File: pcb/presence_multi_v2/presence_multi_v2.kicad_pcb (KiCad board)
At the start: 2 copper layers, 27 parts, among them J1 USB_C_Receptacle_USB2.0_16P, J2 TC2050, J3 Conn_01x06_Socket, U2 AMS1117-3.3, U3 CH340E, Y1 Wurth 830050789

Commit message: replaced ASM1117 with LDL1117, removed 8 pin socket, added 3 4-pin JST-PH connectors
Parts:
- removed ES1: ENS160+AHT21, Connector_PinSocket_2.54mm:PinSocket_1x08_P2.54mm_Vertical
- removed U2: AMS1117-3.3, Package_TO_SOT_SMD:SOT-223-3_TabPin2
- added I2C_Ext1: JST-PH 1x4 2.0, Connector_JST:JST_PH_B4B-PH-K_1x04_P2.00mm_Vertical, F.Cu at (126.5, 125.0)
- added I2C_Ext2: JST-PH 1x4 2.0, Connector_JST:JST_PH_B4B-PH-K_1x04_P2.00mm_Vertical, F.Cu at (136.3, 125.0)
- added I2C_Ext3: JST-PH 1x4 2.0, Connector_JST:JST_PH_B4B-PH-K_1x04_P2.00mm_Vertical, F.Cu at (146.3, 125.0)
- added IC1: LDL1117S33R, theorlangur:LDL1117S33R, F.Cu at (138.0, 100.0)
- C5: value 22u -> 10u
- moved C5 12.0 mm to (132.7, 101.2)
- moved C4 1.25 mm to (143.7, 98.4)
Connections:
- C4 pad 1: /LDO_IN -> GND
- C4 pad 2: GND -> /LDO_IN
- MCU1 pad 20: /I_AIR1 -> unconnected-(MCU1-P1.07/AIN3-Pad20)

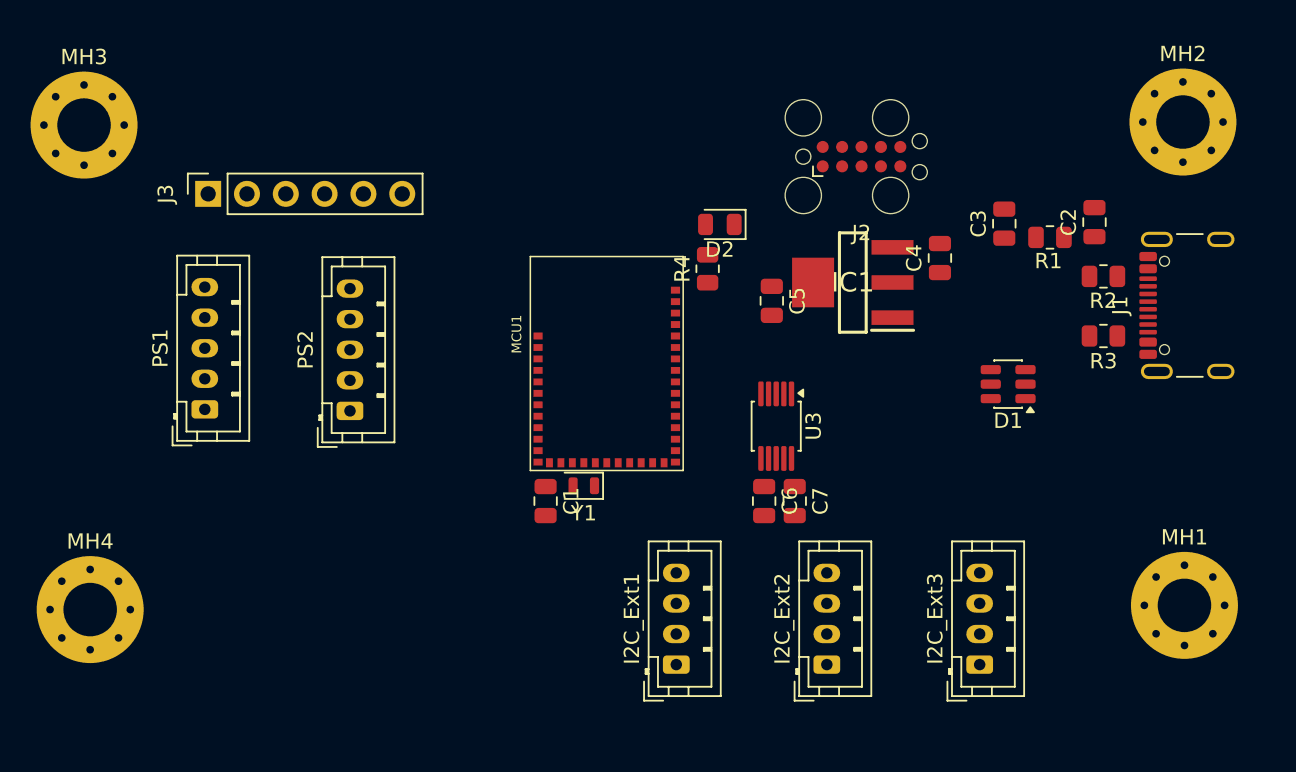
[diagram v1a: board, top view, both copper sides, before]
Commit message: added buttons, configured PCB settings
removed layers
configured pre-defined ruls (constraints)
added default sizes
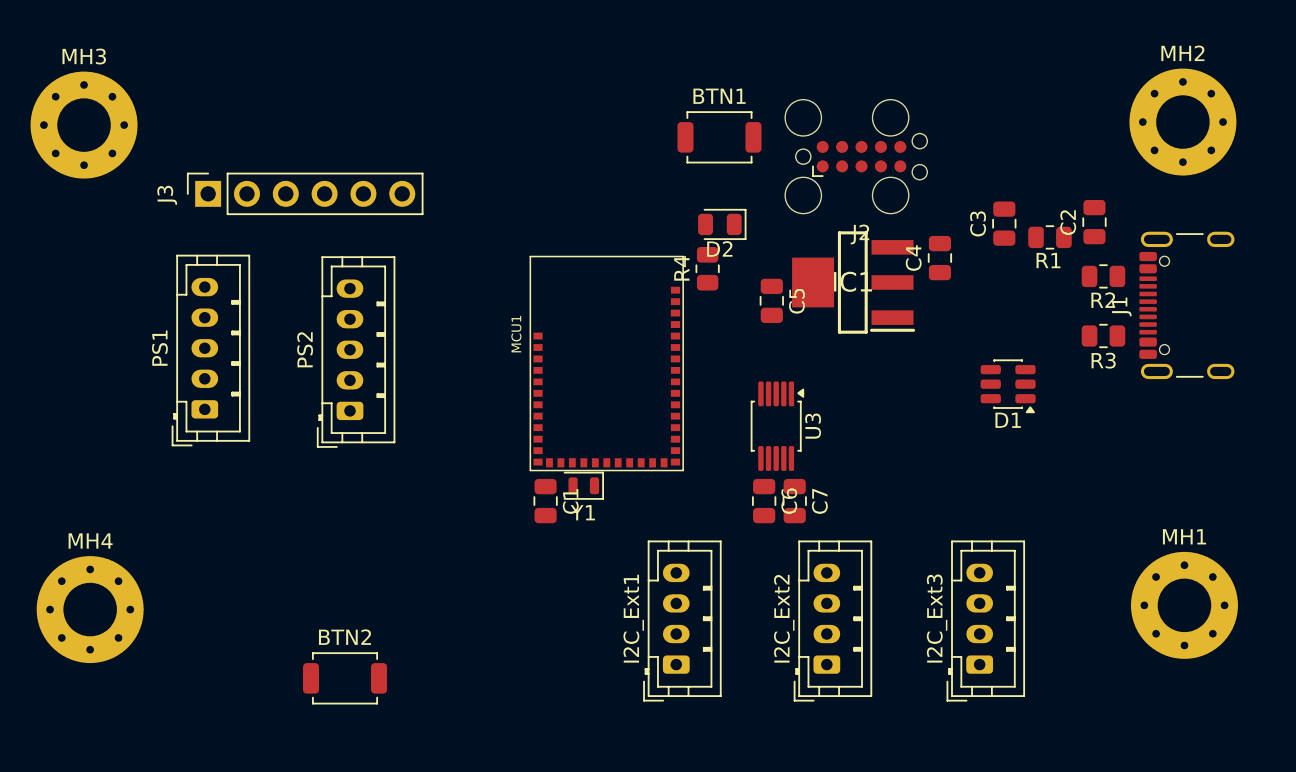
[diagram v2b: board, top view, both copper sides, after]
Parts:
- added BTN1: nRST, Button_Switch_SMD:SW_SPST_TS-1088-xR020, F.Cu at (129.3, 90.5)
- added BTN2: MCUBoot, Button_Switch_SMD:SW_SPST_TS-1088-xR020, F.Cu at (104.8, 125.9)
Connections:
- D1 pad 4: /USBD- -> /USBD+
- D1 pad 6: /USBD+ -> /USBD-
- MCU1 pad 17: unconnected-(MCU1-P0.00-Pad17) -> /BTN_MCUBoot
- U3 pad 1: /USBD- -> /USBD+
- U3 pad 2: /USBD+ -> /USBD-
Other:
- rule pad_to_mask_clearance: 0 -> 0.1

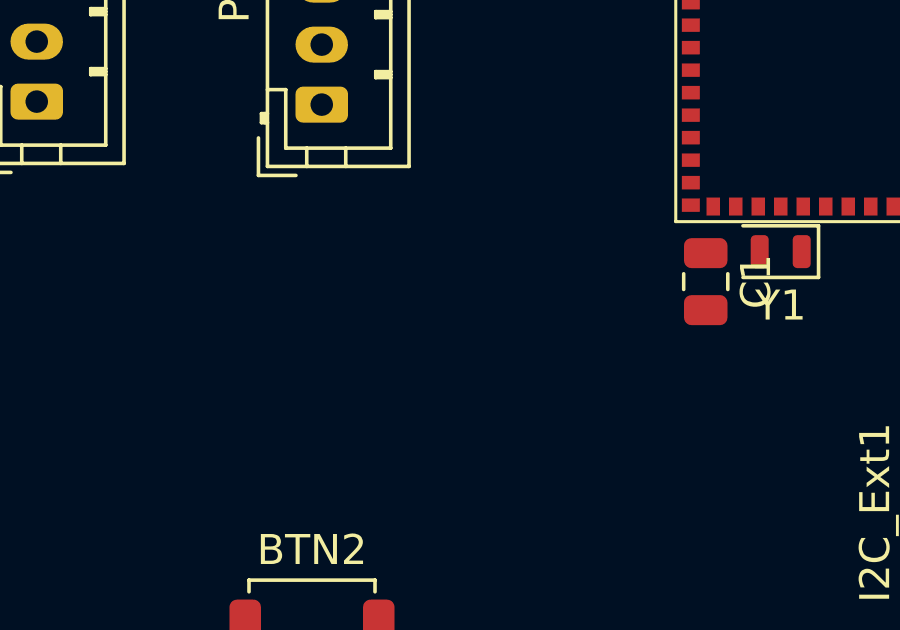
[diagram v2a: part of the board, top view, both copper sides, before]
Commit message: added a dedicated button for zigbee
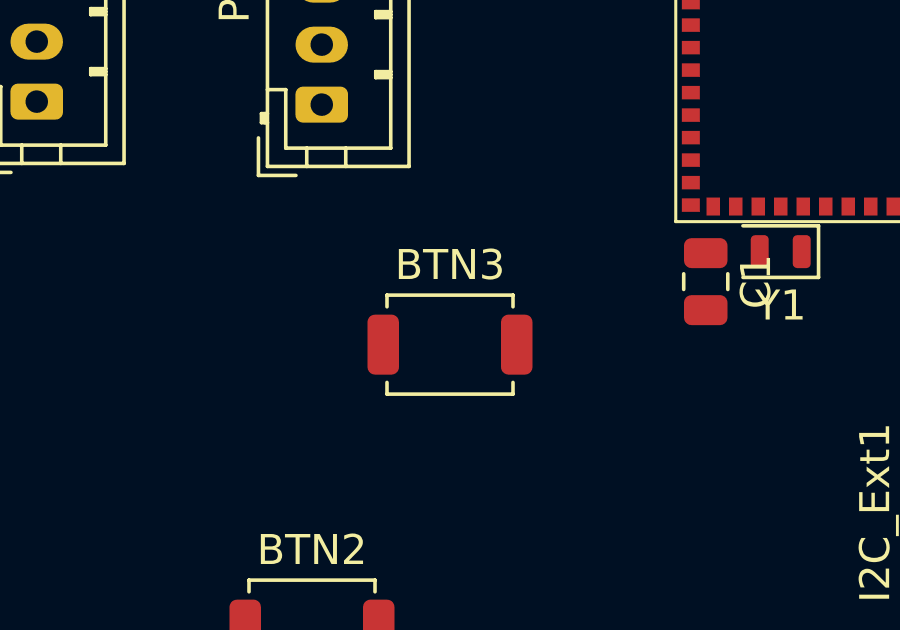
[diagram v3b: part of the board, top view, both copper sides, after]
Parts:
- added BTN3: ZigbeeBtn, Button_Switch_SMD:SW_SPST_TS-1088-xR020, F.Cu at (109.4, 116.4)
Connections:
- MCU1 pad 18: unconnected-(MCU1-P0.01-Pad18) -> /BTN_ZB
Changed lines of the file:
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@@
 	(net 44 "/UART00_RTS")
 	(net 45 "/UART00_RX")
-	(net 46 "unconnected-(MCU1-P0.01-Pad18)")
+	(net 46 "/BTN_ZB")
 	(net 47 "unconnected-(MCU1-P2.03-Pad13)")
 	(net 48 "unconnected-(MCU1-P1.03{slash}NFC2{slash}CLK-Pad14)")
@@
 			(size 0.6 0.45)
 			(layers "F.Cu" "F.Mask" "F.Paste")
-			(net 46 "unconnected-(MCU1-P0.01-Pad18)")
+			(net 46 "/BTN_ZB")
 			(pinfunction "P0.01")
-			(pintype "passive+no_connect")
+			(pintype "passive")
 			(solder_mask_margin 0.0508)
 		)
@@
 			(offset
 				(xyz 0 0 0)
+			)
+			(scale
+				(xyz 1 1 1)
+			)
+			(rotate
+				(xyz 0 0 0)
+			)
+		)
+	)
+	(footprint "Button_Switch_SMD:SW_SPST_TS-1088-xR020"
+		(layer "F.Cu")
+		(at 109.375 116.4)
+		(descr "SMD Tactile Switch, 3.9x3x2 mm, https://lcsc.com/datasheet/lcsc_datasheet_2504101957_XUNPU-TS-1088-AR02016_C720477.pdf")
+		(tags "Tactile Switch")
+		(property "Reference" "BTN3"
+			(at 0 -2.65 0)
+			(layer "F.SilkS")
+			(effects
+				(font
+					(size 1 1)
+					(thickness 0.15)
+				)
+			)
+		)
+		(property "Value" "ZigbeeBtn"
+			(at 0 2.65 0)
+			(layer "F.Fab")
+			(effects
+				(font
+					(size 1 1)
+					(thickness 0.15)
+				)
+			)
+		)
+		(property "Datasheet" "~"
+			(at 0 0 0)
+			(unlocked yes)
+			(layer "F.Fab")
+			(hide yes)
+			(effects
+				(font
+					(size 1.27 1.27)
+					(thickness 0.15)
+				)
+			)
+		)
+		(property "Description" "Push button switch, generic, two pins"
+			(at 0 0 0)
+			(unlocked yes)
+			(layer "F.Fab")
+			(hide yes)
+			(effects
+				(font
+					(size 1.27 1.27)
+					(thickness 0.15)
+				)
+			)
+		)
+		(sheetname "/")
+		(sheetfile "presence_multi_v2.kicad_sch")
+		(attr smd)
+		(fp_line
+			(start -2.1 -1.65)
+			(end 2.1 -1.65)
+			(stroke
+				(width 0.12)
+				(type solid)
+			)
+			(layer "F.SilkS")
+		)
+		(fp_line
+			(start -2.1 -1.26)
+			(end -2.1 -1.65)
+			(stroke
+				(width 0.12)
+				(type solid)
+			)
+			(layer "F.SilkS")
+		)
+		(fp_line
+			(start -2.1 1.26)
+			(end -2.1 1.65)
+			(stroke
+				(width 0.12)
+				(type solid)
+			)
+			(layer "F.SilkS")
+		)
+		(fp_line
+			(start -2.1 1.65)
+			(end 2.1 1.65)
+			(stroke
+				(width 0.12)
+				(type solid)
+			)
+			(layer "F.SilkS")
+		)
+		(fp_line
+			(start 2.1 -1.65)
+			(end 2.1 -1.26)
+			(stroke
+				(width 0.12)
+				(type solid)
+			)
+			(layer "F.SilkS")
+		)
+		(fp_line
+			(start 2.1 1.65)
+			(end 2.1 1.26)
+			(stroke
+				(width 0.12)
+				(type solid)
+			)
+			(layer "F.SilkS")
+		)
+		(fp_line
+			(start -3 -1.75)
+			(end -3 1.75)
+			(stroke
+				(width 0.05)
+				(type solid)
+			)
+			(layer "F.CrtYd")
+		)
+		(fp_line
+			(start -3 1.75)
+			(end 3 1.75)
+			(stroke
+				(width 0.05)
+				(type solid)
+			)
+			(layer "F.CrtYd")
+		)
+		(fp_line
+			(start 3 -1.75)
+			(end -3 -1.75)
+			(stroke
+				(width 0.05)
+				(type solid)
+			)
+			(layer "F.CrtYd")
+		)
+		(fp_line
+			(start 3 1.75)
+			(end 3 -1.75)
+			(stroke
+				(width 0.05)
+				(type solid)
+			)
+			(layer "F.CrtYd")
+		)
+		(fp_line
+			(start -1.95 -1.5)
+			(end 1.95 -1.5)
+			(stroke
+				(width 0.1)
+				(type solid)
+			)
+			(layer "F.Fab")
+		)
+		(fp_line
+			(start -1.95 1.5)
+			(end -1.95 -1.5)
+			(stroke
+				(width 0.1)
+				(type solid)
+			)
+			(layer "F.Fab")
+		)
+		(fp_line
+			(start -1.95 1.5)
+			(end 1.95 1.5)
+			(stroke
+				(width 0.1)
+				(type solid)
+			)
+			(layer "F.Fab")
+		)
+		(fp_line
+			(start 1.95 -1.5)
+			(end 1.95 1.5)
+			(stroke
+				(width 0.1)
+				(type solid)
+			)
+			(layer "F.Fab")
+		)
+		(fp_circle
+			(center 0 0)
+			(end 0.9 0)
+			(stroke
+				(width 0.1)
+				(type solid)
+			)
+			(fill no)
+			(layer "F.Fab")
+		)
+		(fp_text user "${REFERENCE}"
+			(at 0 -2.65 0)
+			(layer "F.Fab")
+			(effects
+				(font
+					(size 1 1)
+					(thickness 0.15)
+				)
+			)
+		)
+		(pad "1" smd roundrect
+			(at -2.225 0)
+			(size 1.05 2)
+			(layers "F.Cu" "F.Mask" "F.Paste")
+			(roundrect_rratio 0.2380952381)
+			(net 2 "GND")
+			(pinfunction "1")
+			(pintype "passive")
+		)
+		(pad "2" smd roundrect
+			(at 2.225 0)
+			(size 1.05 2)
+			(layers "F.Cu" "F.Mask" "F.Paste")
+			(roundrect_rratio 0.2380952381)
+			(net 46 "/BTN_ZB")
+			(pinfunction "2")
+			(pintype "passive")
+		)
+		(embedded_fonts no)
+		(model "${KICAD9_3DMODEL_DIR}/Button_Switch_SMD.3dshapes/SW_SPST_TS-1088-xR020.step"
+			(offset
+				(xyz 0 0 0)

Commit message: routing PCB
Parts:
- moved I2C_Ext3 50.1 mm to (96.2, 123.0), turned to 0 degrees
- moved BTN2 33.3 mm to (137.2, 118.5), turned to 180 degrees
- moved BTN3 28.8 mm to (137.2, 123.8), turned to 180 degrees
- moved I2C_Ext2 28.6 mm to (107.8, 123.0), turned to 0 degrees
- moved J3 22.1 mm to (93.0, 116.1), turned to 180 degrees
- moved J2 16.9 mm to (121.7, 93.1), turned to 180 degrees
- moved BTN1 16.7 mm to (112.8, 93.0)
- moved PS1 8.89 mm to (101.0, 115.4)
- moved PS2 8.89 mm to (110.5, 115.5)
- moved I2C_Ext1 7.33 mm to (119.4, 123.0), turned to 0 degrees
- moved D1 5.14 mm to (149.9, 101.8)
- moved MH4 4.98 mm to (90.0, 126.0)
- moved C3 2.79 mm to (150.0, 94.3)
- moved C2 2.52 mm to (152.0, 94.3)
- moved MH3 2.40 mm to (90.0, 89.0)
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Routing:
- net +3V3: track 0.00 -> 43.7 mm, vias 0 -> 2
- net /SWDCLK: track 0.00 -> 28.4 mm, vias 0 -> 2
- net /nRST: track 0.00 -> 25.3 mm
- net /SWDIO: track 0.00 -> 24.6 mm, vias 0 -> 2
- net /USBD-: track 0.00 -> 18.6 mm
- net /USBD+: track 0.00 -> 17.9 mm
- net +VBUS: track 0.00 -> 15.5 mm
- net /UART00_TX: track 0.00 -> 11.8 mm
- net /LDO_IN: track 0.00 -> 11.5 mm
- net /UART00_RX: track 0.00 -> 11.0 mm
- net /UART00_CTS: track 0.00 -> 10.1 mm, vias 0 -> 2
- net /USBCD+: track 0.00 -> 9.46 mm
- net /USBCD-: track 0.00 -> 8.89 mm
- net /UART00_RTS: track 0.00 -> 8.63 mm, vias 0 -> 2
- net /LED0: track 0.00 -> 2.62 mm
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
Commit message: ready version
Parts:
- Y1: footprint Crystal:Crystal_SMD_2012-2Pin_2.0x1.2mm -> theorlangur:Wurth-XTAL-830050789
- moved I2C_Ext1 9.60 mm to (129.0, 123.0)
- moved I2C_Ext2 9.60 mm to (117.3, 123.0)
- moved I2C_Ext3 9.60 mm to (105.8, 123.0)
- moved R2 8.80 mm to (154.2, 108.4)
- moved D1 8.80 mm to (149.7, 110.6)
- moved R1 8.80 mm to (150.7, 105.8)
- moved R3 8.80 mm to (154.2, 112.3)
- moved C2 8.80 mm to (151.8, 103.1)
- moved C3 8.80 mm to (149.8, 103.1)
- moved J1 8.80 mm to (160.8, 110.3)
- moved MCUBoot 6.71 mm to (143.2, 115.5)
- moved Zigbee 6.71 mm to (143.2, 120.8)
- moved MH3 4.30 mm to (92.5, 92.5)
- moved MH4 3.54 mm to (92.5, 123.5)
- moved MH1 2.96 mm to (159.0, 124.0)
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- renumbered BTN2 to MCUBoot, BTN3 to Zigbee, BTN1 to nRST
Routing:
- net +3V3: track 43.7 -> 112.5 mm, vias 2 -> 6
- net /I2C20_SDA: track 0.00 -> 48.5 mm
- net /I2C20_SCL: track 0.00 -> 36.5 mm
- net /EXT0: track 0.00 -> 27.7 mm
- net /EXT1: track 0.00 -> 26.8 mm
- net /EXT2: track 0.00 -> 25.8 mm
- net /EXT3: track 0.00 -> 24.7 mm
- net /BTN_ZB: track 0.00 -> 20.1 mm, vias 0 -> 2
- net /UART20_TX: track 0.00 -> 18.8 mm
- net /UART20_RX: track 0.00 -> 18.3 mm
- net /I_PRESENCE1: track 0.00 -> 17.7 mm, vias 0 -> 2
- net /BTN_MCUBoot: track 0.00 -> 17.1 mm, vias 0 -> 2
- net /UART21_TX: track 0.00 -> 8.21 mm
- net /UART21_RX: track 0.00 -> 7.57 mm
- net /I_PRESENCE2: track 0.00 -> 7.06 mm
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- added copper zone on B.Cu, net GND
- added copper zone on F.Cu, net GND
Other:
- board outline added: 77 x 42 mm

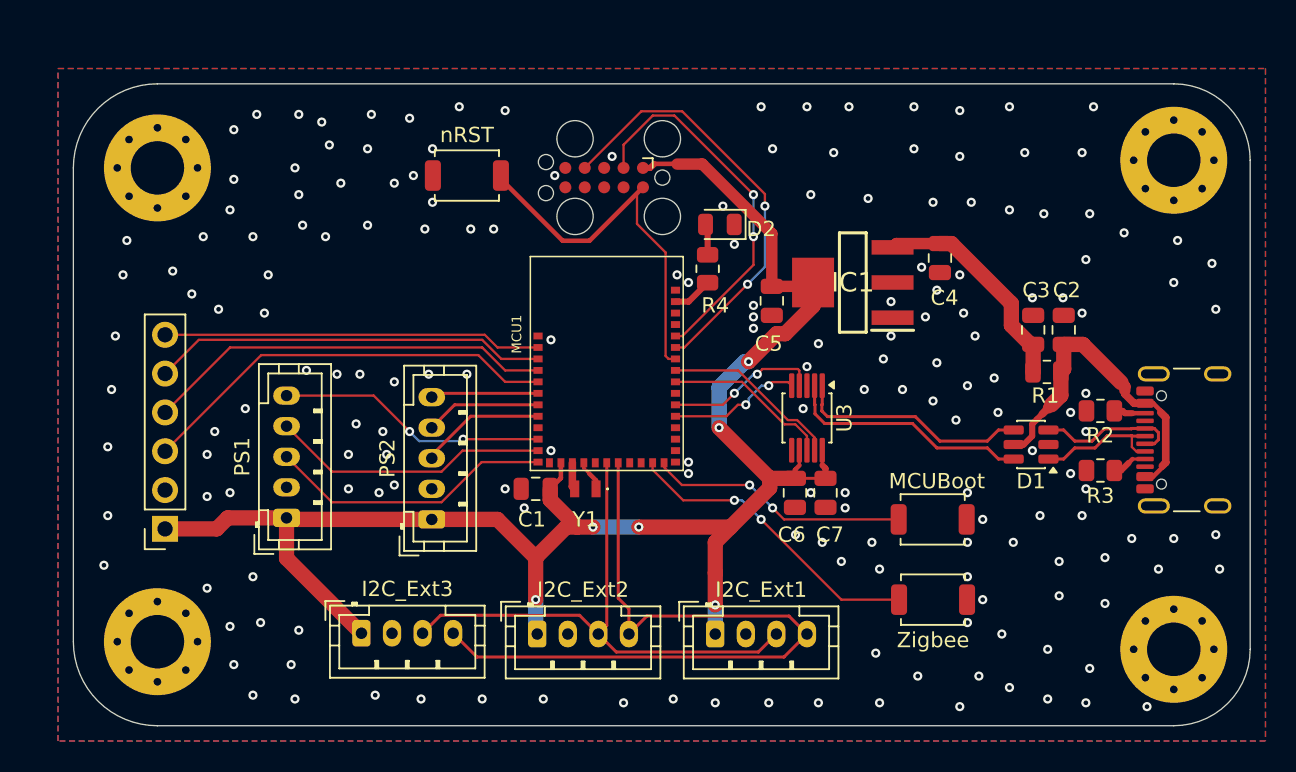
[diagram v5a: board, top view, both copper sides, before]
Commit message: adjusted edge cuts (same radius used); adjusted some labels
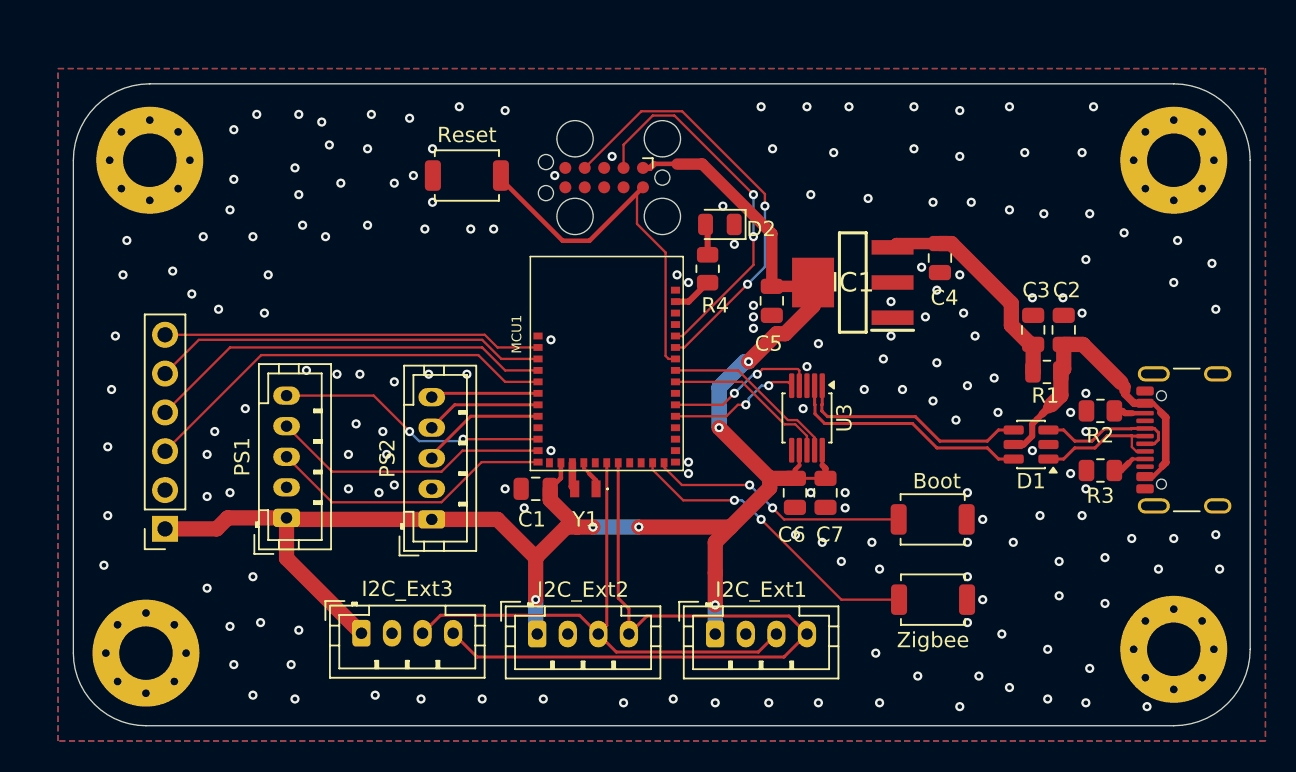
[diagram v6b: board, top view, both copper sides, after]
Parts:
- moved MH4 1.06 mm to (91.8, 124.2)
- moved MH3 0.71 mm to (92.0, 92.0)
- renumbered MCUBoot to Boot, nRST to Reset
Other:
- outline, holes or cut-outs redrawn
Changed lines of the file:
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@@
 		)
 		(pad_to_mask_clearance 0.1)
-		(solder_mask_min_width 0.1)
 		(allow_soldermask_bridges_in_footprints no)
 		(tenting front back)
@@
 		(descr "SMD Tactile Switch, 3.9x3x2 mm, https://lcsc.com/datasheet/lcsc_datasheet_2504101957_XUNPU-TS-1088-AR02016_C720477.pdf")
 		(tags "Tactile Switch")
-		(property "Reference" "nRST"
+		(property "Reference" "Reset"
 			(at 0 -2.65 0)
 			(layer "F.SilkS")
@@
 	(footprint "MountingHole:MountingHole_3.5mm_Pad_Via"
 		(layer "F.Cu")
-		(at 92.5 92.5)
+		(at 92 92)
 		(descr "Mounting Hole 3.5mm, generated by kicad-footprint-generator mountinghole.py")
 		(tags "mountinghole")
@@
 	(footprint "MountingHole:MountingHole_3.5mm_Pad_Via"
 		(layer "F.Cu")
-		(at 92.5 123.5)
+		(at 91.75 124.25)
 		(descr "Mounting Hole 3.5mm, generated by kicad-footprint-generator mountinghole.py")
 		(tags "mountinghole")
@@
 		(descr "SMD Tactile Switch, 3.9x3x2 mm, https://lcsc.com/datasheet/lcsc_datasheet_2504101957_XUNPU-TS-1088-AR02016_C720477.pdf")
 		(tags "Tactile Switch")
-		(property "Reference" "MCUBoot"
+		(property "Reference" "Boot"
 			(at -0.275 2.5 0)
 			(layer "F.SilkS")
@@
 	)
 	(gr_arc
-		(start 92.5 129)
-		(mid 88.610913 127.389087)
-		(end 87 123.5)
+		(start 91.75 129)
+		(mid 88.391243 127.608757)
+		(end 87 124.25)
 		(stroke
 			(width 0.05)
@@
 	)
 	(gr_line
-		(start 92.5 87)
+		(start 92 87)
 		(end 159 87)
 		(stroke
@@
 	)
 	(gr_line
-		(start 92.5 129)
+		(start 91.75 129)
 		(end 159 129)
 		(stroke
@@
 	)
 	(gr_arc
-		(start 87 92.5)
-		(mid 88.610913 88.610913)
-		(end 92.5 87)
+		(start 87 92)
+		(mid 88.464466 88.464466)
+		(end 92 87)
 		(stroke
 			(width 0.05)
@@
 	)
 	(gr_line
-		(start 87 92.5)
-		(end 87 123.5)
+		(start 87 92)
+		(end 87 124.25)
 		(stroke
 			(width 0.05)
